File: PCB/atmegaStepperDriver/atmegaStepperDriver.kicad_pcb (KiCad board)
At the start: 2 copper layers, 70 parts, among them J1 Screw_Terminal_01x02, J2 Motor Output, J3 Screw_Terminal_01x02, J4 Conn_01x05_Socket, J5 Conn_01x02_Socket, Q1 TIP42C, Q10 BC547, Q11 BC557, Q12 BC547, Q13 BC557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

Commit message: communication pins;
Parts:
- moved C4 17.6 mm to (98.5, 122.6)
- moved C2 14.6 mm to (92.4, 122.5)
- moved R2 14.1 mm to (52.7, 108.0), turned to 0 degrees
- moved R12 13.9 mm to (66.7, 92.7), turned to 0 degrees
- moved R14 13.9 mm to (79.4, 92.7), turned to 0 degrees
- moved R16 13.5 mm to (92.1, 92.7), turned to 0 degrees
- moved R18 13.5 mm to (104.8, 92.7), turned to 0 degrees
- moved C3 9.94 mm to (88.6, 122.5)
- moved D1 9.44 mm to (74.6, 122.6)
- moved D9 6.00 mm to (94.0, 137.8)
- moved J4 6.00 mm to (82.5, 137.8)
- moved JP1 4.84 mm to (109.9, 135.9)
- moved U2 4.07 mm to (90.5, 132.7)
- moved JP2 4.03 mm to (114.3, 136.5)
- moved J1 3.90 mm to (110.8, 126.4)
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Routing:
- net Gate 3: track 11.0 -> 0.00 mm
- net Gate 4: track 11.0 -> 0.00 mm
- net Gate 1: track 10.3 -> 0.00 mm
- net Gate 2: track 10.3 -> 0.00 mm
- net Net-(D1-A): track 0.90 -> 0.00 mm
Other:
- board outline added: 51.4 x 94.6 mm
- board text added: "atMega Stepper Driver Developer board V0.0.4"
- board text added: "bruh"

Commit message: General design ready; footprints ready; V0.0.5
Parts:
- added D2: D, Diode_THT:D_A-405_P7.62mm_Horizontal, F.Cu at (110.5, 59.1)
- added D3: D, Diode_THT:D_A-405_P7.62mm_Horizontal, F.Cu at (114.3, 59.1)
- added D4: D, Diode_THT:D_A-405_P7.62mm_Horizontal, F.Cu at (103.5, 124.5)
- added D5: D, Diode_THT:D_A-405_P7.62mm_Horizontal, F.Cu at (103.5, 134.6)
- added J6: I2C Communication pins, Connector_PinHeader_2.54mm:PinHeader_1x04_P2.54mm_Vertical, F.Cu at (74.9, 135.3)
- added J9: Stepper communication pins, Connector_PinHeader_2.54mm:PinHeader_1x04_P2.54mm_Vertical, F.Cu at (78.7, 135.3)
- J1: value Screw_Terminal_01x02 -> General power
- J3: value Screw_Terminal_01x02 -> Motor power
- J5: value Conn_01x02_Socket -> Reset Header
- moved C14 31.3 mm to (96.5, 135.3)
- moved J5 22.9 mm to (90.2, 135.3), turned to 90 degrees
- moved R2 16.5 mm to (67.3, 115.6)
- moved R1 11.1 mm to (114.9, 104.8), turned to 180 degrees
- moved D1 9.22 mm to (80.6, 115.6)
- moved JP3 9.09 mm to (114.3, 48.3)
- moved C4 8.32 mm to (93.9, 115.6), turned to 180 degrees
- moved U2 8.28 mm to (86.1, 125.7)
- moved D9 8.12 mm to (88.9, 131.4)
- moved D10 7.93 mm to (92.7, 131.4)
- moved C5 7.82 mm to (96.5, 125.7)
- moved J4 7.74 mm to (78.1, 131.4)
- moved JP8 7.25 mm to (109.9, 101.0)
- moved C2 6.67 mm to (88.9, 128.2), turned to 90 degrees
- moved JP7 6.55 mm to (98.4, 101.0)
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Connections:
- C2 pad 2: Net-(D10-K) -> VCCInput
- C5 pad 1: Net-(D10-K) -> VCCInput
- J1 pad 1: GND -> Net-(D4-K)
- J1 pad 2: VCCInput -> Net-(D5-A)
- JP2 pad 1: Net-(D10-K) -> VCCInput
- JP3 pad 1: Motor Power -> Net-(D3-A)
- JP4 pad 1: Motor Ground -> Net-(D2-K)
- JP7 pad 2: unconnected-(JP7-B-Pad2) -> Net-(JP7-B)
- JP8 pad 2: unconnected-(JP8-B-Pad2) -> Jumper To lower pisn
- U1 pad 13: unconnected-(U1-PD7-Pad13) -> Rotation
- U1 pad 17: unconnected-(U1-PB3-Pad17) -> Net-(JP7-B)
- U1 pad 27: unconnected-(U1-PC4-Pad27) -> SDA
- U1 pad 28: unconnected-(U1-PC5-Pad28) -> SCL
- U1 pad 4: unconnected-(U1-PD2-Pad4) -> Step
- U1 pad 5: unconnected-(U1-PD3-Pad5) -> Jumper To lower Pins
- U1 pad 6: unconnected-(U1-PD4-Pad6) -> Error
- U2 pad 1: Net-(D10-K) -> VCCInput
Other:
- board size 51.4 x 94.6 mm -> 51.4 x 92.1 mm
- board text added: "General power"
- board text added: "Motor from general"
- board text added: "Motor power"
- board text added: "atMega Stepper Driver Developer board V0.1.0"
- board text removed: "atMega Stepper Driver Developer board V0.0.4"
- board text removed: "bruh"

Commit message: All general connections ready; further check needed; V0.0.6
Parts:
- removed D10, D9: D, Diode_THT:D_A-405_P7.62mm_Horizontal
- C5: footprint Capacitor_THT:CP_Radial_Tantal_D9.0mm_P5.00mm -> Capacitor_THT:CP_Radial_D10.0mm_P5.00mm
- moved C14 15.4 mm to (81.6, 131.5)
- moved C1-1 8.31 mm to (113.7, 113.7), turned to 180 degrees
- moved C1-2 8.17 mm to (105.5, 113.7), turned to 0 degrees
- moved D2 7.62 mm to (110.5, 51.4), turned to -90 degrees
- moved Y1 5.62 mm to (106.7, 109.2), turned to 0 degrees
- moved C7 2.54 mm to (84.8, 55.9), turned to -90 degrees
- moved U2 0.90 mm to (85.4, 126.4)
- moved R4 0.06 mm to (68.3, 74.4)
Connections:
- D2 pad 2: Motor Ground -> GND
- JP8 pad 2: Jumper To lower pisn -> Jumper To lower Pins
- Q2 pad 3: Motor Ground -> GND
- Q6 pad 3: Motor Ground -> GND
- Q7 pad 3: Motor Ground -> GND
- Q8 pad 3: Motor Ground -> GND
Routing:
- net Motor Power: track 0.00 -> 48.4 mm
- net output A: track 0.00 -> 44.8 mm
- net output B: track 0.00 -> 44.7 mm
- net RST: track 0.00 -> 43.8 mm, vias 0 -> 2
- net Rotation: track 0.00 -> 43.5 mm, vias 0 -> 1
- net output !B: track 0.00 -> 41.6 mm
- net Net-(U1-XTAL1/PB6): track 0.00 -> 38.0 mm
- net Jumper To lower Pins: track 0.00 -> 37.7 mm, vias 0 -> 1
- net output !A: track 0.00 -> 35.1 mm
- net SCL: track 0.00 -> 33.8 mm
- net VCCInput: track 0.00 -> 33.3 mm
- net SDA: track 0.00 -> 33.3 mm
- net Net-(JP5-B): track 0.00 -> 31.5 mm
- net +5V: track 41.9 -> 73.2 mm
- net Net-(U1-XTAL2/PB7): track 0.00 -> 25.4 mm
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- added copper zone on B.Cu, net GND
- added copper zone on F.Cu, net GND

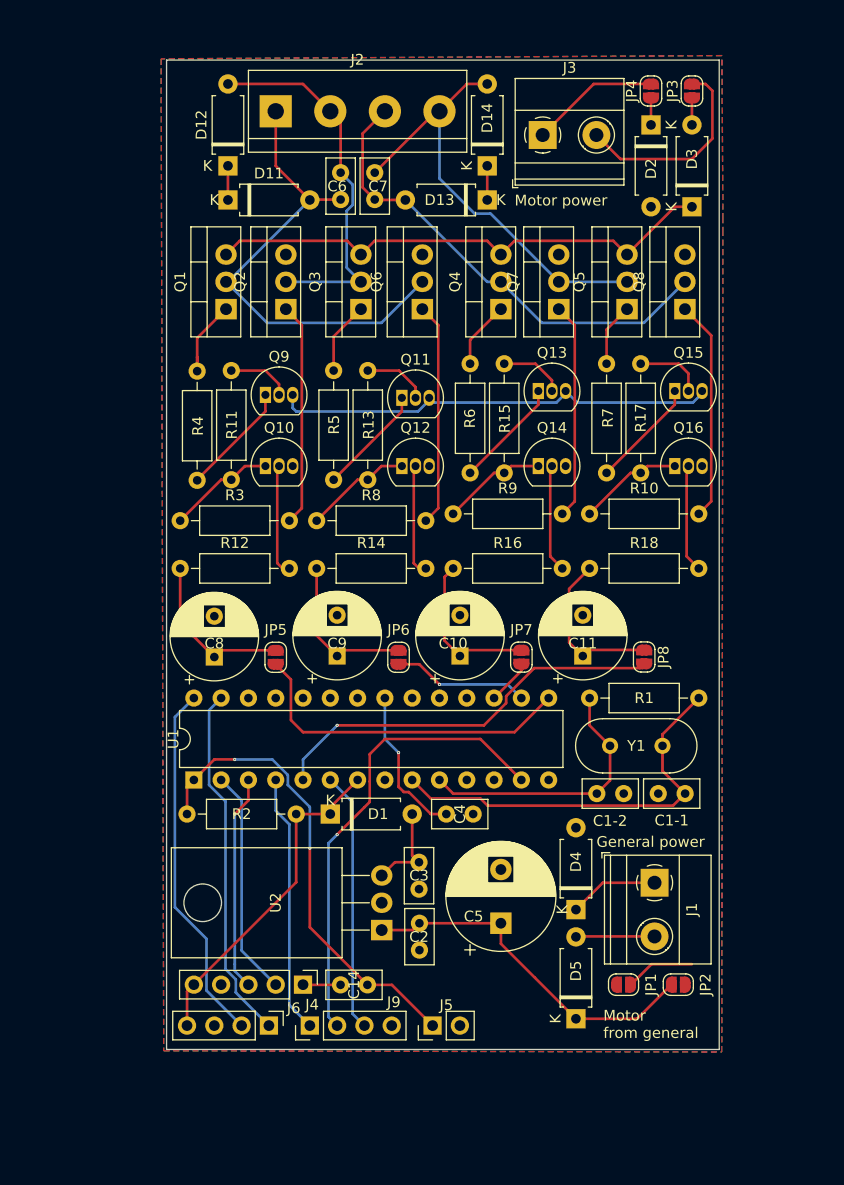
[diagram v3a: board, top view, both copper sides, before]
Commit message: Footprint done; ready for testing; drc clear; Gerber files;V0.7.1;
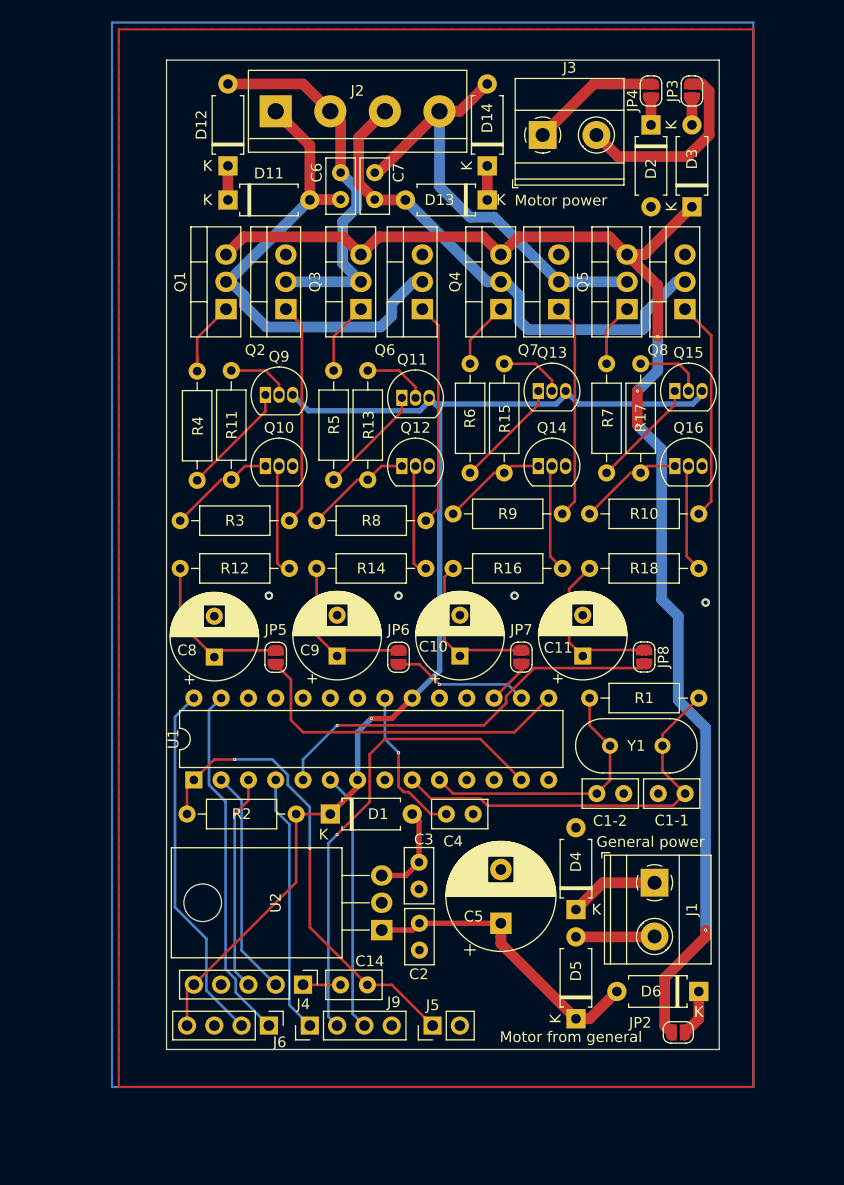
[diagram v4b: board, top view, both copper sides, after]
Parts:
- removed JP1: SolderJumper_2_Open, Jumper:SolderJumper-2_P1.3mm_Open_RoundedPad1.0x1.5mm
- added D6: D, Diode_THT:D_A-405_P7.62mm_Horizontal, F.Cu at (114.9, 132.1)
- moved JP2 4.44 mm to (113.0, 135.9)
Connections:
- JP2 pad 1: VCCInput -> Motor Power
- JP2 pad 2: Motor Power -> Net-(D6-K)
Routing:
- net Motor Power: track 48.4 -> 128.1 mm, vias 0 -> 4
- net +5V: track 73.2 -> 113.1 mm, vias 0 -> 1
- net Motor Ground: track 6.50 -> 0.00 mm
- net VCCInput: track 33.3 -> 28.0 mm
- net Net-(D6-K): track 0.00 -> 4.33 mm
- net output B: track 44.7 -> 47.7 mm
- net output A: track 44.8 -> 46.3 mm
- net Net-(J3-Pin_2): track 19.1 -> 18.1 mm
- net Net-(Q1-B): track 8.93 -> 8.15 mm
- net output !A: track 35.1 -> 35.7 mm
- net GND: vias 0 -> 4
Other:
- board text added: "atMega Stepper Driver Developer board V0.7.1"
- board text removed: "atMega Stepper Driver Developer board V0.1.0"

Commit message: fixed old design flaw; full redisgn; Few things to be done; V0.8.0;
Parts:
- removed C10, C11, C8, C9: C, Capacitor_THT:CP_Radial_D8.0mm_P3.80mm
- removed J4: Conn_01x05_Socket, Connector_PinHeader_2.54mm:PinHeader_1x05_P2.54mm_Vertical
- removed JP8: SolderJumper_2_Open, Jumper:SolderJumper-2_P1.3mm_Open_RoundedPad1.0x1.5mm
- added C2-1: C, Capacitor_THT:CP_Radial_D8.0mm_P3.80mm, F.Cu at (72.4, 99.7)
- added C2-2: C, Capacitor_THT:CP_Radial_D8.0mm_P3.80mm, F.Cu at (81.2, 99.7)
- added C2-3: C, Capacitor_THT:CP_Radial_D8.0mm_P3.80mm, F.Cu at (90.1, 99.7)
- added C2-4: C, Capacitor_THT:CP_Radial_D8.0mm_P3.80mm, F.Cu at (99.0, 99.7)
- added D7: LED, LED_THT:LED_D5.0mm, F.Cu at (112.4, 119.1)
- added J8: Conn_01x06_Socket, Connector_PinHeader_2.54mm:PinHeader_1x06_P2.54mm_Vertical, F.Cu at (95.2, 130.8)
- added JP1: SolderJumper_2_Open, Jumper:SolderJumper-2_P1.3mm_Open_RoundedPad1.0x1.5mm, F.Cu at (69.9, 94.0)
- added R19: 220, Resistor_THT:R_Axial_DIN0207_L6.3mm_D2.5mm_P10.16mm_Horizontal, F.Cu at (104.8, 98.4)
- added REF**: MountingHole_3.2mm_M3_DIN965, MountingHole:MountingHole_3.2mm_M3_DIN965, F.Cu at (113.7, 48.3)
- added REF**: MountingHole_3.2mm_M3_DIN965, MountingHole:MountingHole_3.2mm_M3_DIN965, F.Cu at (113.7, 134.0)
- added REF**: MountingHole_3.2mm_M3_DIN965, MountingHole:MountingHole_3.2mm_M3_DIN965, F.Cu at (69.2, 134.0)
- added REF**: MountingHole_3.2mm_M3_DIN965, MountingHole:MountingHole_3.2mm_M3_DIN965, F.Cu at (69.2, 48.3)
- Q12, Q16: value BC547 -> TIP41C; footprint Package_TO_SOT_THT:TO-92_Inline -> Package_TO_SOT_THT:TO-220-3_Vertical
- Q13: value BC557 -> TIP42C; footprint Package_TO_SOT_THT:TO-92_Inline -> Package_TO_SOT_THT:TO-220-3_Vertical
- Q5: value TIP42C -> BC547; footprint Package_TO_SOT_THT:TO-220-3_Vertical -> Package_TO_SOT_THT:TO-92_Inline
- Q6: value TIP41C -> BC547; footprint Package_TO_SOT_THT:TO-220-3_Vertical -> Package_TO_SOT_THT:TO-92_Inline
- Q7: value TIP41C -> BC557; footprint Package_TO_SOT_THT:TO-220-3_Vertical -> Package_TO_SOT_THT:TO-92_Inline
- R14, R15, R18: value 1k -> 50
- R7, R8, R9: value 50 -> 1k
- U2: footprint Package_TO_SOT_THT:TO-220-3_Horizontal_TabDown -> Package_TO_SOT_THT:TO-220-3_Vertical
- moved JP5 60.5 mm to (113.7, 54.0), turned to 90 degrees
- moved JP2 53.7 mm to (79.4, 94.0), turned to 180 degrees
- moved JP3 52.6 mm to (88.2, 94.0), turned to 180 degrees
- moved JP6 52.3 mm to (109.9, 54.0), turned to 90 degrees
- moved JP4 47.6 mm to (97.1, 94.0), turned to 180 degrees
- moved JP7 28.9 mm to (114.3, 125.1), turned to 90 degrees
- moved J5 22.7 mm to (68.6, 128.3)
- moved R16 19.0 mm to (109.2, 84.5), turned to 90 degrees
- moved C2 18.5 mm to (71.8, 121.3), turned to 180 degrees
- moved U2 18.3 mm to (69.2, 117.8), turned to 0 degrees
- moved D6 16.8 mm to (106.7, 117.5)
- moved Q7 14.7 mm to (100.3, 83.2), turned to 0 degrees
- moved Q8 14.6 mm to (99.1, 69.2)
- moved Q16 14.1 mm to (110.5, 69.2), turned to 90 degrees
- moved Q14 14.1 mm to (112.4, 76.6)
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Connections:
- JP2 pad 1: Motor Power -> Gate 2
- JP2 pad 2: Net-(D6-K) -> Net-(JP2-B)
- JP3 pad 1: Net-(D3-A) -> Gate 3
- JP3 pad 2: Net-(J3-Pin_2) -> Net-(JP3-B)
- JP4 pad 1: Net-(D2-K) -> Gate 4
- JP4 pad 2: Net-(J3-Pin_1) -> Jumper To lower Pins
- JP5 pad 1: Gate 1 -> Net-(D3-A)
- JP5 pad 2: Net-(JP5-B) -> Net-(J3-Pin_2)
- JP6 pad 1: Gate 2 -> Net-(D2-K)
- JP6 pad 2: Net-(JP6-B) -> Net-(J3-Pin_1)
- JP7 pad 1: Gate 3 -> Motor Power
- JP7 pad 2: Net-(JP7-B) -> Net-(D6-K)
- Q12 pad 1: Net-(Q12-C) -> Net-(Q12-B)
- Q12 pad 2: Net-(Q12-B) -> output A
- Q13 pad 1: Net-(Q13-C) -> Net-(Q13-B)
- Q13 pad 2: Net-(Q13-B) -> output !B
- Q13 pad 3: +5V -> Motor Power
- Q16 pad 1: Net-(Q16-C) -> Net-(Q16-B)
- Q16 pad 2: Net-(Q16-B) -> output B
- Q5 pad 1: Net-(Q5-B) -> Net-(Q5-C)
- Q5 pad 2: output !B -> Net-(Q5-B)
- Q5 pad 3: Motor Power -> GND
- Q6 pad 1: Net-(Q6-B) -> Net-(Q6-C)
- Q6 pad 2: output A -> Net-(Q6-B)
- Q7 pad 1: Net-(Q7-B) -> Net-(Q7-C)
- Q7 pad 2: output !B -> Net-(Q7-B)
- Q7 pad 3: GND -> +5V
- Q8 pad 2: output B -> output !B
- R10 pad 1: Net-(Q16-C) -> Net-(Q7-C)
- R13 pad 1: Net-(Q12-C) -> Gate 2
- R13 pad 2: Net-(Q11-B) -> Net-(Q6-B)
- R14 pad 1: Gate 2 -> Net-(Q11-C)
- R15 pad 1: Net-(Q14-C) -> Net-(Q13-B)
- R15 pad 2: Net-(Q13-B) -> Net-(Q14-C)
- R16 pad 1: Gate 3 -> Net-(Q14-C)
- R16 pad 2: Net-(Q14-B) -> Net-(Q15-B)
- R17 pad 1: Net-(Q16-C) -> Gate 4
- R17 pad 2: Net-(Q15-B) -> Net-(Q14-B)
- R18 pad 1: Gate 4 -> Net-(Q15-C)
- R3 pad 1: Net-(Q10-C) -> Net-(Q9-C)
- R4 pad 2: Net-(Q9-C) -> Net-(Q10-C)
- R5 pad 1: Net-(Q11-C) -> Net-(Q3-B)
- R5 pad 2: Net-(Q3-B) -> Net-(Q6-C)
- R6 pad 2: Net-(Q13-C) -> Net-(Q5-C)
- R7 pad 1: Net-(Q15-C) -> Net-(Q5-C)
- R7 pad 2: Net-(Q5-B) -> Net-(Q7-B)
- R8 pad 1: Net-(Q12-C) -> Net-(Q6-C)
- R8 pad 2: Net-(Q6-B) -> Net-(Q11-B)
- R9 pad 1: Net-(Q14-C) -> Gate 3
- R9 pad 2: Net-(Q7-B) -> Net-(Q5-B)
- U1 pad 11: unconnected-(U1-PD5-Pad11) -> Net-(U1-PD5)
- U1 pad 15: Net-(JP5-B) -> Net-(JP1-B)
- U1 pad 16: Net-(JP6-B) -> Net-(JP2-B)
- U1 pad 17: Net-(JP7-B) -> Net-(JP3-B)
- U1 pad 2: TX -> RXD
- U1 pad 3: RX -> TXD
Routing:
- net Net-(JP1-B): track 0.00 -> 41.1 mm, vias 0 -> 1
- net RXD: track 0.00 -> 32.7 mm, vias 0 -> 1
- net Net-(JP5-B): track 31.5 -> 0.00 mm
- net Net-(JP2-B): track 0.00 -> 29.9 mm, vias 0 -> 1
- net TXD: track 0.00 -> 25.9 mm, vias 0 -> 1
- net +5V: track 113.1 -> 135.7 mm, vias 1 -> 4
- net VCCInput: track 28.0 -> 50.2 mm
- net TX: track 21.2 -> 0.00 mm
- net Net-(D7-A): track 0.00 -> 20.2 mm
- net RX: track 20.1 -> 0.00 mm, vias 1 -> 0
- net Net-(U1-PD5): track 0.00 -> 19.1 mm
- net RST: track 43.8 -> 25.8 mm, vias 2 -> 0
- net Net-(JP3-B): track 0.00 -> 17.0 mm
- net Rotation: track 43.5 -> 28.5 mm
- net Net-(JP6-B): track 12.7 -> 0.00 mm, vias 1 -> 0
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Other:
- board size 51.4 x 92.1 mm -> 50.8 x 92.1 mm
- board text added: "General Power"
- board text removed: "General power"
- board text removed: "Motor from general"
- board text removed: "atMega Stepper Driver Developer board V0.7.1"

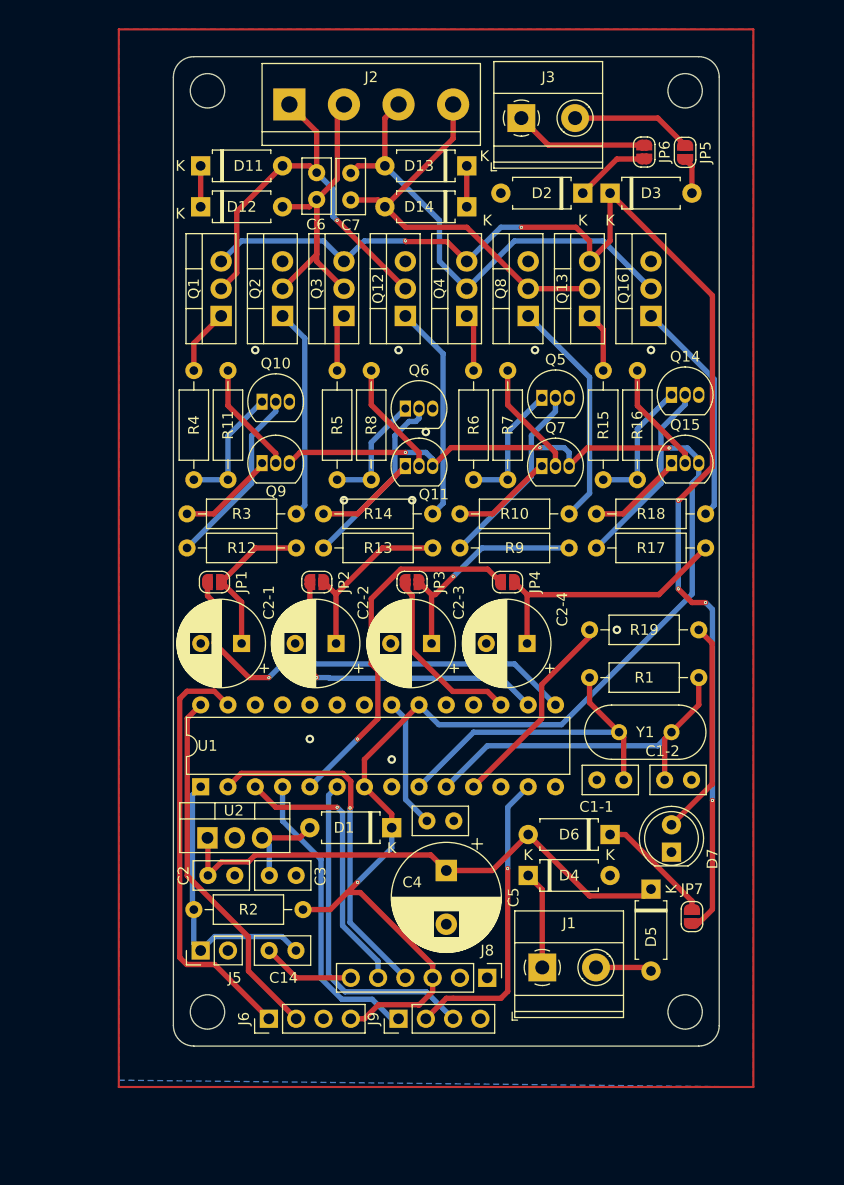
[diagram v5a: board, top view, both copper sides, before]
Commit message: traces fixed; fan added; V0.8.1
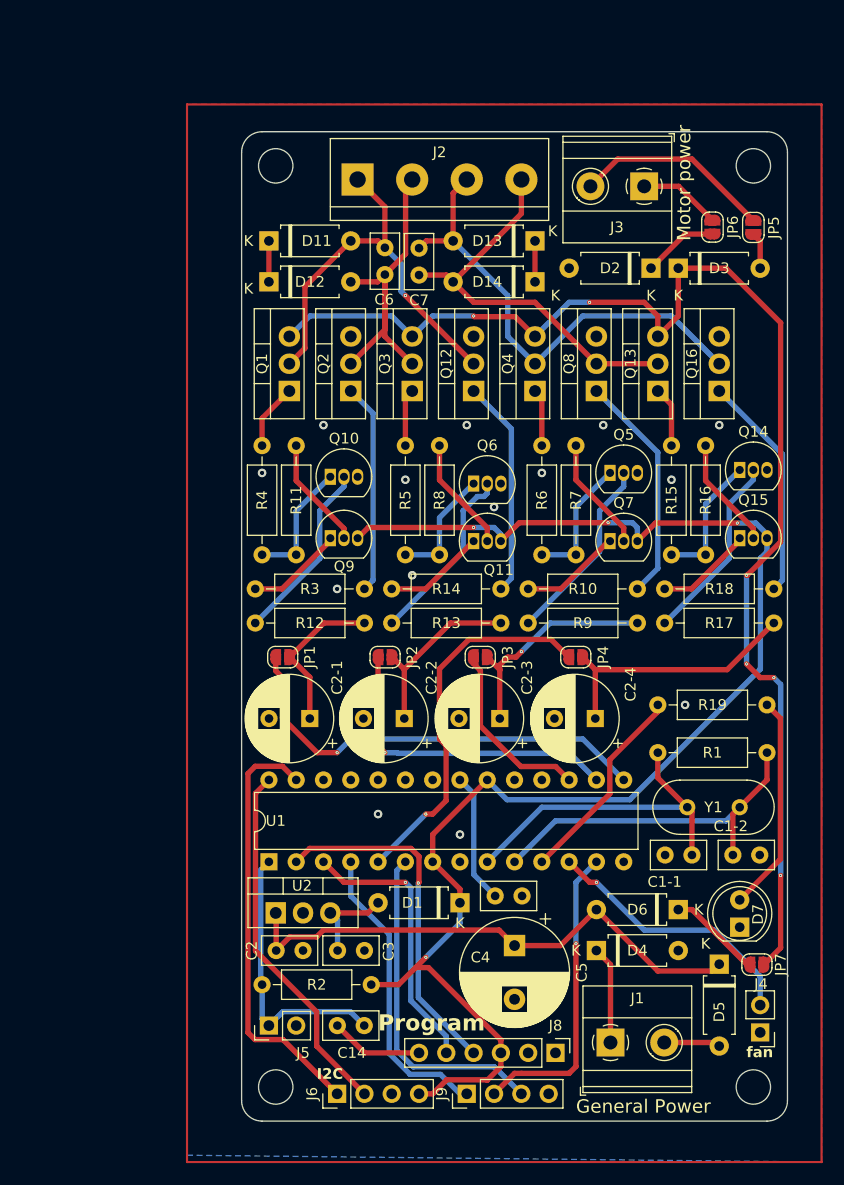
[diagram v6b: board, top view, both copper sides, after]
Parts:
- added J4: Conn_01x02_Pin, Connector_PinHeader_2.54mm:PinHeader_1x02_P2.54mm_Vertical, F.Cu at (120.7, 135.9)
- moved J3 13.1 mm to (109.9, 57.1), turned to 180 degrees
- moved C2 9.44 mm to (78.1, 128.3)
- moved C2-2 9.44 mm to (87.5, 106.7)
- moved C2-3 9.44 mm to (96.4, 106.7)
- moved C2-4 9.44 mm to (105.3, 106.7)
- moved D12 9.44 mm to (74.9, 66.0)
- moved C2-1 9.44 mm to (78.7, 106.7)
- moved C3 9.44 mm to (83.8, 128.3)
- moved D4 9.44 mm to (105.4, 128.3)
- moved J1 9.44 mm to (106.7, 136.8)
- moved Q10 9.44 mm to (80.6, 84.2)
- moved C5 9.44 mm to (97.8, 127.8)
- moved C7 9.44 mm to (88.9, 65.4)
- moved D11 9.44 mm to (74.9, 62.2)
- moved D7 9.44 mm to (118.7, 126.1)
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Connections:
- U1 pad 12: unconnected-(U1-PD6-Pad12) -> Fan
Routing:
- net Fan: track 0.00 -> 24.9 mm, vias 0 -> 1
- net Net-(J3-Pin_2): track 11.3 -> 18.6 mm
- net Net-(J3-Pin_1): track 12.5 -> 7.65 mm
- net Net-(D6-K): track 11.0 -> 8.79 mm
- net Motor Power: track 124.8 -> 123.7 mm
- net Jumper To lower Pins: track 34.0 -> 35.1 mm
- net GND: vias 14 -> 18
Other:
- board text added: "I2C"
- board text added: "Program"
- board text added: "atMega Stepper Driver V0.8.0"
- board text added: "fan"
